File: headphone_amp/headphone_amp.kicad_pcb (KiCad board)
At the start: 2 copper layers, 100 x 50 mm, 40 parts, among them J1 Molex_SL_01x02_Male, J2 Molex_SL_01x02_Male, J3 Molex_SL_01x03_Male, J4 Molex_SL_01x03_Male, Q1 PZTA42, Q2 PZTA92, Q3 PZTA42, Q4 PZTA92, U1 NE5532

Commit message: adjust output connector location slightly
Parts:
- moved J3 1.50 mm to (186.0, 115.5)
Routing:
- net /right_out: track 12.5 -> 14.0 mm
- net /left_out: track 10.2 -> 11.7 mm
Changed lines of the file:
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@@
     (thickness 1.6)
     (drawings 8)
-    (tracks 197)
+    (tracks 198)
     (zones 0)
     (modules 40)
@@
   )
   (module Connector_Molex_SL:Molex_SL_A-70553-0002_1x03_P2.54mm_Horizontal (layer F.Cu)
-    (at 187.5 115.5 270)
+    (at 186 115.5 270)
     (descr "Molex SL Modular Connectors, old/engineering part number: A-70553-0002 example for new part number: 70543-0002, 3 Pins (https://www.molex.com/pdm_docs/sd/705530001_sd.pdf), generated with kicad-footprint-generator")
     (tags "connector Molex SL top entry")
@@
   (segment (start 121.255 133) (end 127.864 126.391) (width 0.254) (layer F.Cu) (net 21))
   (segment (start 113.75 133) (end 121.255 133) (width 0.254) (layer F.Cu) (net 21))
-  (segment (start 192 122.31) (end 192 126.802944) (width 0.4064) (layer F.Cu) (net 22))
-  (segment (start 187.73 118.04) (end 192 122.31) (width 0.4064) (layer F.Cu) (net 22))
-  (segment (start 192 126.802944) (end 192 128.5) (width 0.4064) (layer F.Cu) (net 22))
-  (segment (start 187.5 118.04) (end 187.73 118.04) (width 0.4064) (layer F.Cu) (net 22))
+  (segment (start 187.5 118.04) (end 186 118.04) (width 0.4064) (layer F.Cu) (net 22))
+  (segment (start 192 128.5) (end 192 122.31) (width 0.4064) (layer F.Cu) (net 22))
+  (segment (start 187.73 118.04) (end 187.5 118.04) (width 0.4064) (layer F.Cu) (net 22))
+  (segment (start 192 122.31) (end 187.73 118.04) (width 0.4064) (layer F.Cu) (net 22))
   (segment (start 191.5 111.5) (end 187.5 115.5) (width 0.4064) (layer F.Cu) (net 23))
   (segment (start 191.5 107) (end 191.5 111.5) (width 0.4064) (layer F.Cu) (net 23))
+  (segment (start 187.5 115.5) (end 186 115.5) (width 0.4064) (layer F.Cu) (net 23))
   (segment (start 144.8 115.425) (end 145 115.625) (width 0.4064) (layer F.Cu) (net 24))
   (segment (start 144.8 113.15) (end 144.8 115.425) (width 0.4064) (layer F.Cu) (net 24))

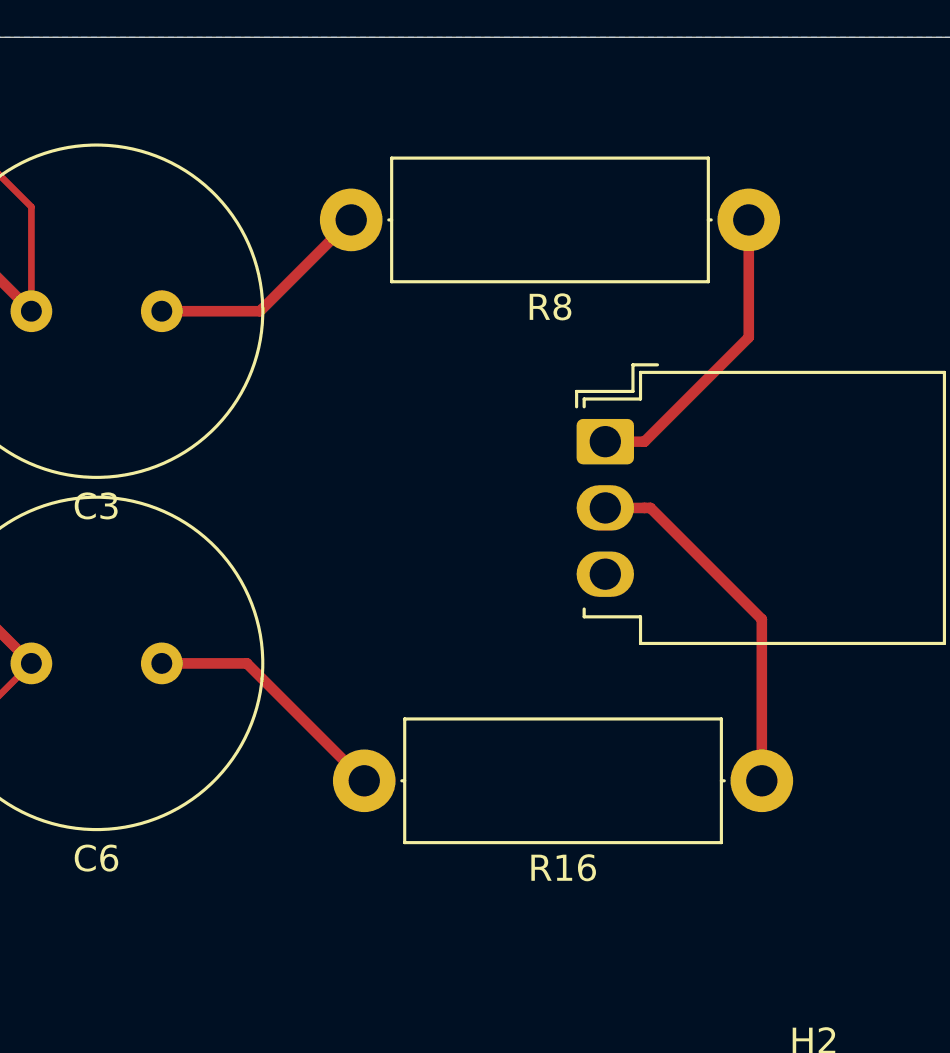
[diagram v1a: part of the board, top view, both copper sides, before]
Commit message: Remove output resistors
- remove output resistors for zero ohm output impedance
- add 10k pulldown/bleeder resistors on output to prevent output cap
charging with no load
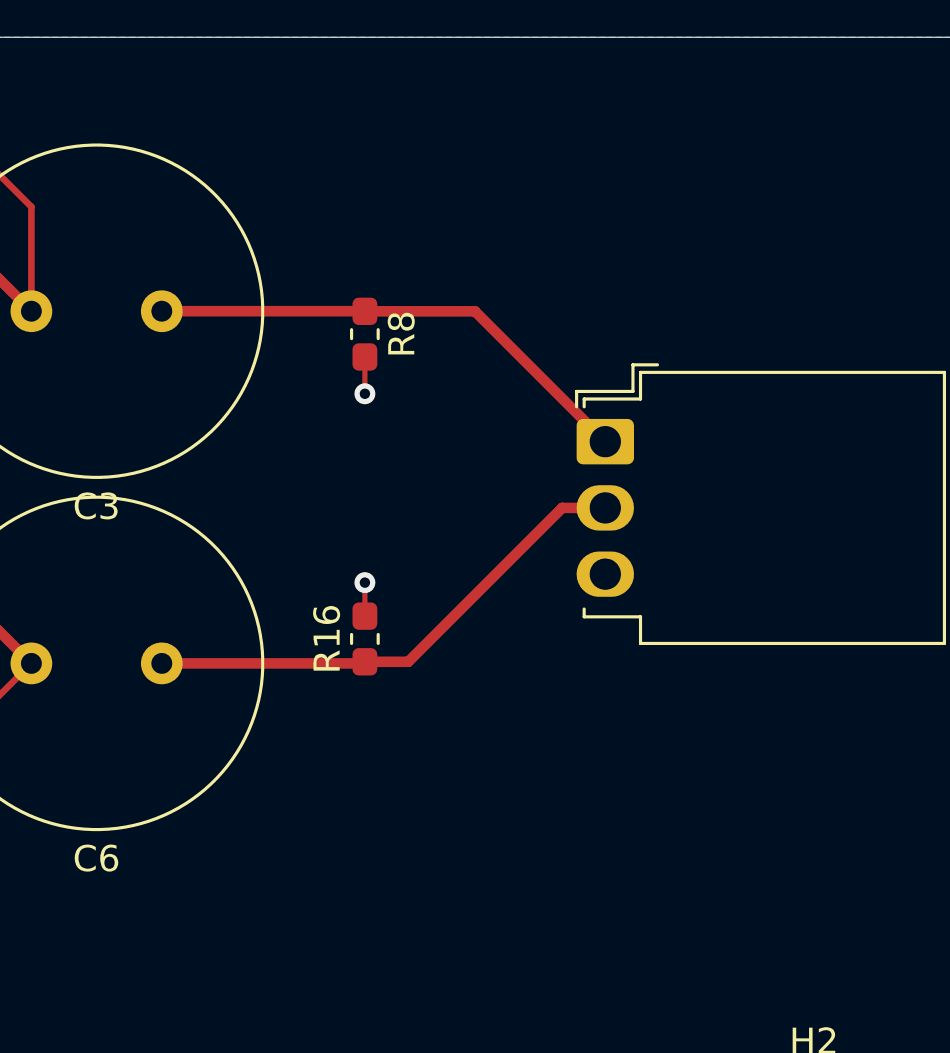
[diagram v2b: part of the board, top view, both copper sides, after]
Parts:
- R16, R8: value 47 1W -> 10k; footprint Resistor_THT:R_Axial_DIN0414_L11.9mm_D4.5mm_P15.24mm_Horizontal -> Resistor_SMD:R_0603_1608Metric_Pad1.05x0.95mm_HandSolder
- moved R16 16.2 mm to (176.8, 123.1), turned to 90 degrees
- moved R8 15.4 mm to (176.8, 111.4), turned to 270 degrees
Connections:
- C3 pad 1: Net-(C3-Pad1) -> /left_out
- C6 pad 1: Net-(C6-Pad1) -> /right_out
- R16 pad 2: Net-(C6-Pad1) -> GNDA
- R8 pad 2: Net-(C3-Pad1) -> GNDA
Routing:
- net Net-(C6-Pad1): track 9.62 -> 0.00 mm
- net Net-(C3-Pad1): track 8.71 -> 0.00 mm
- net /left_out: track 11.7 -> 19.1 mm
- net /right_out: track 14.0 -> 19.5 mm
- net GNDA: track 6.46 -> 9.16 mm, vias 2 -> 4
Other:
- board text added: "TODO check height of all components, especially output caps choose orientation and rearrange connectors? connect output ground to star ground"
- board text removed: "TODO check height of all components, especially output caps choose orientation and rearrange connectors?"
